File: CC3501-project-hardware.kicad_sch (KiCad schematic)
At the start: 29 parts, among them J1 USB_C_Receptacle_USB2.0_16P, J3 Conn_01x03_Socket, Q1 AO3400A, U1 RP2040, U4 SY8089A1AAC

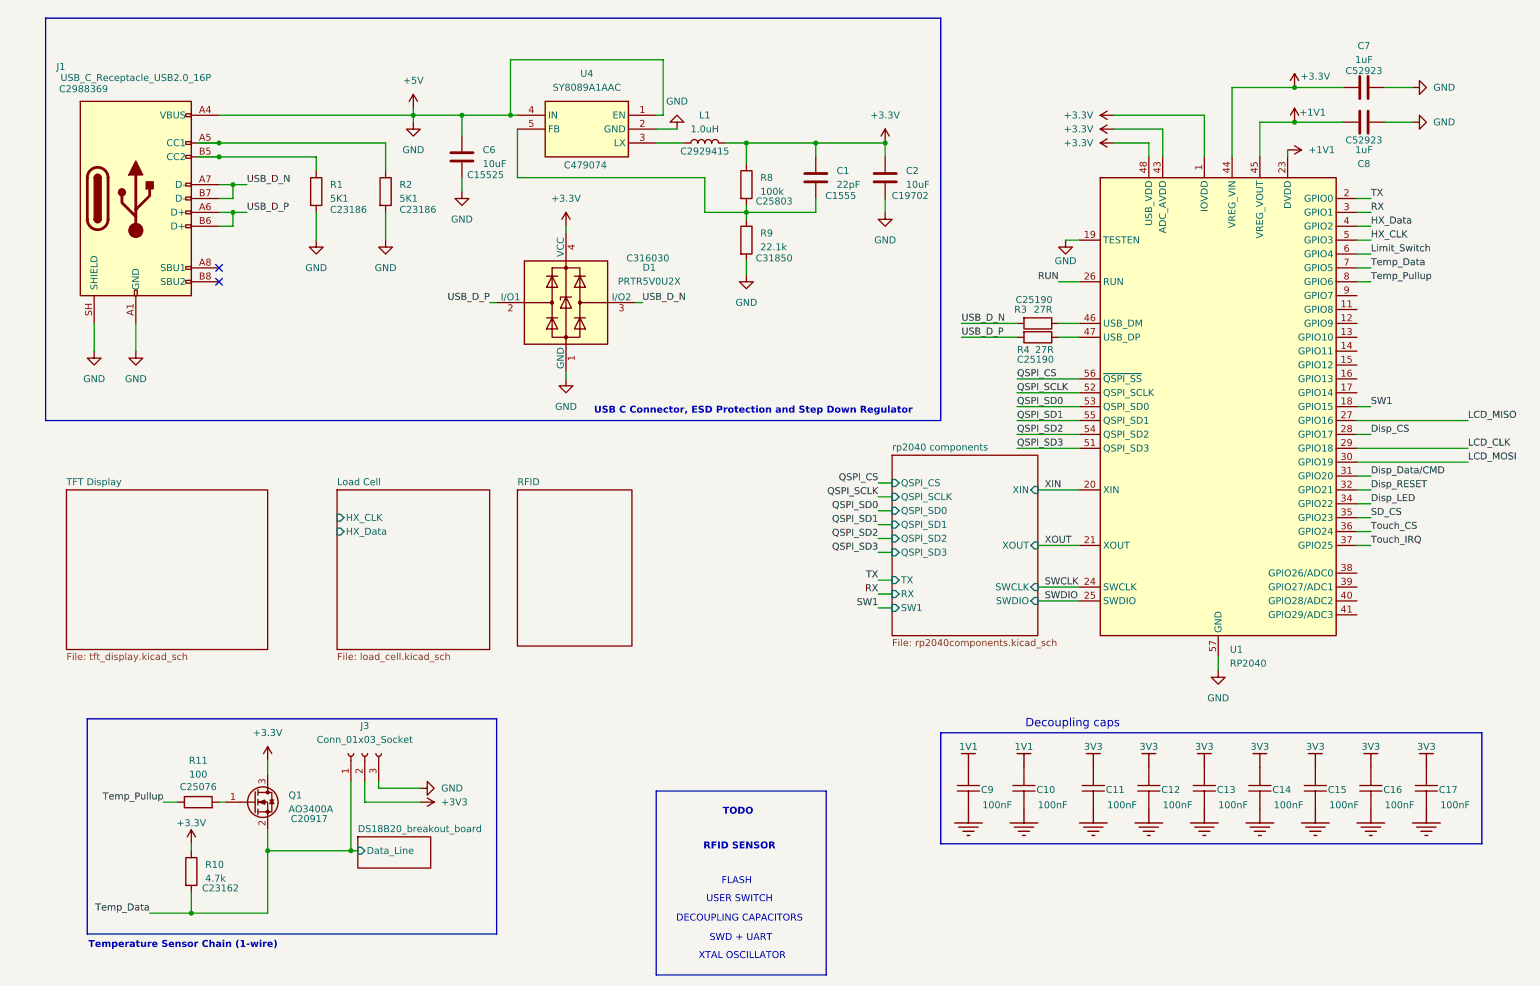
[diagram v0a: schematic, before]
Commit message: Attached part number to components.
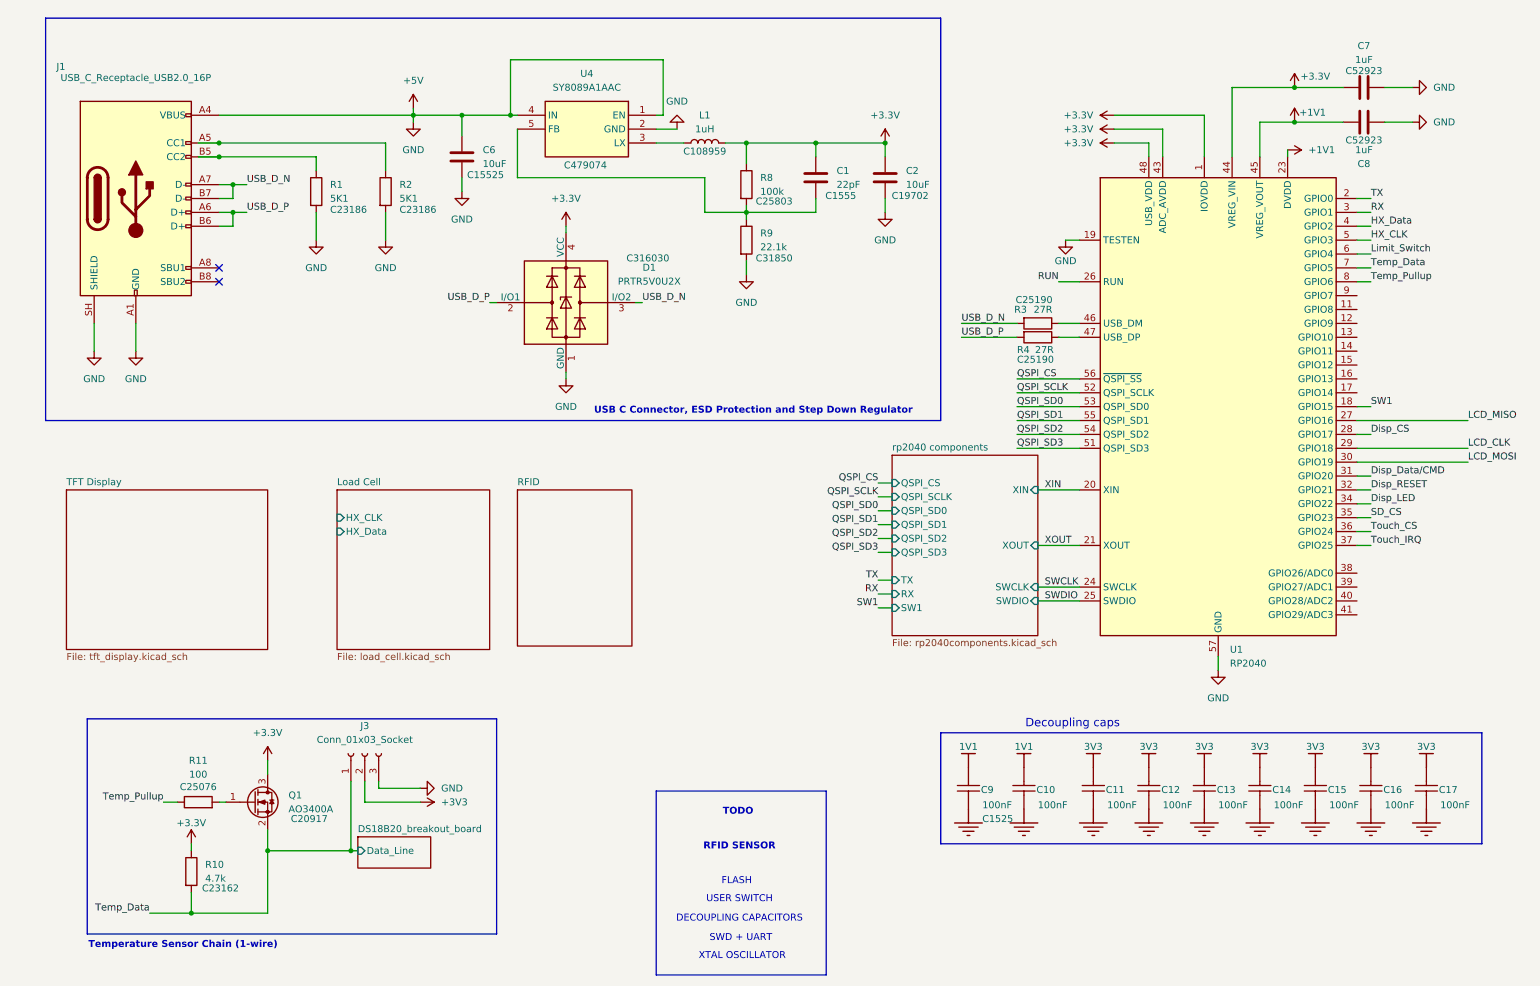
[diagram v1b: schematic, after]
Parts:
- C10, C11, C12, C13, C14, C15, C16, C17, C9: value CL05B104KO5NNNC -> 100nF
- J1: footprint Connector_USB:USB_C_Receptacle_G-Switch_GT-USB-7010ASV -> Connector_PinSocket_2.54mm:PinSocket_1x03_P2.54mm_Vertical; LCSC PN C2988369 -> (none)
- L1: value 1.0uH -> 1uH; footprint SamacSys_Parts:IND-SMD_L4.5-W4.0 -> Inductor_SMD:L_0603_1608Metric; LCSC PN C2929415 -> C108959
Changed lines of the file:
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@@
 			)
 		)
-		(property "Value" "CL05B104KO5NNNC"
+		(property "Value" "100nF"
 			(at 196.85 166.37 0)
 			(hide yes)
@@
 			)
 		)
-		(property "Value" "CL05B104KO5NNNC"
+		(property "Value" "100nF"
 			(at 270.51 166.37 0)
 			(hide yes)
@@
 	)
 	(symbol
+		(lib_name "root_1_CAP-NP-2_James Cook University_1")
 		(lib_id "James Cook University:root_1_CAP-NP-2_James Cook University")
 		(at 182.88 158.75 0)
@@
 			)
 		)
-		(property "Value" "CL05B104KO5NNNC"
+		(property "Value" "100nF"
 			(at 186.69 166.37 0)
 			(hide yes)
@@
 		)
 		(property "LCSC PN" "C1525"
-			(at 182.88 158.75 0)
-			(hide yes)
+			(at 185.42 160.528 0)
 			(show_name no)
 			(do_not_autoplace no)
@@
 					(size 1.27 1.27)
 				)
+				(justify left)
 			)
 		)
@@
 			)
 		)
-		(property "Value" "CL05B104KO5NNNC"
+		(property "Value" "100nF"
 			(at 240.03 166.37 0)
 			(hide yes)
@@
 			)
 		)
-		(property "Value" "CL05B104KO5NNNC"
+		(property "Value" "100nF"
 			(at 209.55 166.37 0)
 			(hide yes)
@@
 			)
 		)
-		(property "Value" "CL05B104KO5NNNC"
+		(property "Value" "100nF"
 			(at 229.87 166.37 0)
 			(hide yes)
@@
 			)
 		)
-		(property "Value" "CL05B104KO5NNNC"
+		(property "Value" "100nF"
 			(at 219.71 166.37 0)
 			(hide yes)
@@
 			)
 		)
-		(property "Value" "CL05B104KO5NNNC"
+		(property "Value" "100nF"
 			(at 250.19 166.37 0)
 			(hide yes)
@@
 			)
 		)
-		(property "Value" "CL05B104KO5NNNC"
+		(property "Value" "100nF"
 			(at 260.35 166.37 0)
 			(hide yes)
@@
 			)
 		)
-		(property "Value" "1.0uH"
+		(property "Value" "1uH"
 			(at 134.62 34.29 90)
 			(show_name no)
@@
 			)
 		)
-		(property "Footprint" "SamacSys_Parts:IND-SMD_L4.5-W4.0"
+		(property "Footprint" "Inductor_SMD:L_0603_1608Metric"
 			(at 134.62 36.83 0)
 			(hide yes)
@@
 			)
 		)
-		(property "LCSC PN" "C2929415"
+		(property "LCSC PN" "C108959"
 			(at 134.62 38.354 90)
 			(show_name no)
@@
 			)
 		)
-		(property "Footprint" "Connector_USB:USB_C_Receptacle_G-Switch_GT-USB-7010ASV"
+		(property "Footprint" "Connector_PinSocket_2.54mm:PinSocket_1x03_P2.54mm_Vertical"
 			(at 34.29 46.99 0)
 			(hide yes)
@@
 			)
 		)
-		(property "LCSC PN" "C2988369"
+		(property "LCSC PN" ""
 			(at 25.4 27.686 0)
 			(show_name no)

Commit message: Fix ERC errors.
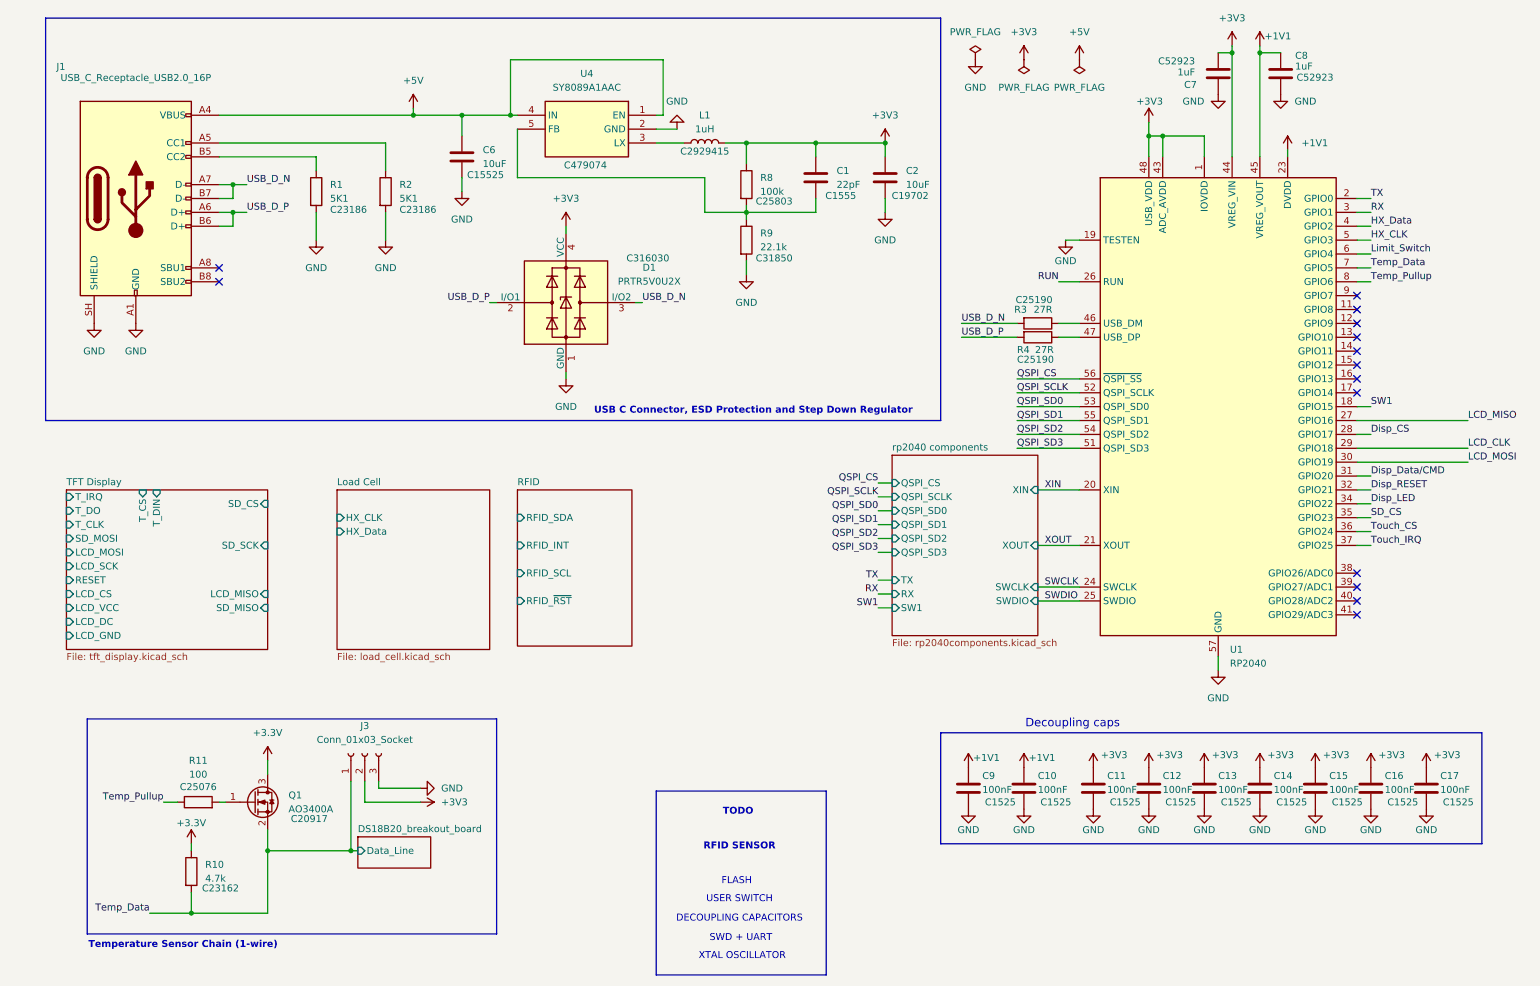
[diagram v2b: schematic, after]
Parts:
- removed C10, C11, C12, C13, C14, C15, C16, C17, C9: 100nF, Capacitor_SMD:C_0402_1005Metric, symbol James Cook University:root_1_CAP-NP-2_James Cook University
- added C10, C11, C12, C13, C14, C15, C16, C17, C9: 100nF, Capacitor_SMD:C_0402_1005Metric, symbol Device:C
- L1: footprint Inductor_SMD:L_0603_1608Metric -> SamacSys_Parts:IND-SMD_L4.5-W4.0; LCSC PN C108959 -> C2929415
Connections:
- net +1V1: now also C8.2, C10.1, C9.1; no longer C8.1
- net +3.3V: no longer C1.1, C2.1, C7.2, D1.4 (VCC), L1.1, R8.1, U1.1 (IOVDD), U1.10 (IOVDD), U1.22 (IOVDD), U1.33 (IOVDD), U1.42 (IOVDD), U1.43 (ADC_AVDD), U1.44 (VREG_VIN), U1.48 (USB_VDD), U1.49 (IOVDD)
- net +3V3: now also C1.1, C2.1, C7.2, D1.4 (VCC), L1.1, R8.1, U1.1 (IOVDD), U1.10 (IOVDD), U1.22 (IOVDD), U1.33 (IOVDD), U1.42 (IOVDD), U1.43 (ADC_AVDD), U1.44 (VREG_VIN), U1.48 (USB_VDD), U1.49 (IOVDD), C11.1, C12.1, C13.1, C14.1, C15.1, C16.1, C17.1
- net +5V: no longer C2.2, C6.2, C7.1, C8.2, D1.1 (GND), J1.A1 (GND), J1.A12 (GND), J1.B1 (GND), J1.B12 (GND), J1.SH (SHIELD), J3.3 (Pin_3), R1.2, R2.2, R9.2, U1.19 (TESTEN), U1.57 (GND), U4.2 (GND)
- new net GND: C10.2, C11.2, C12.2, C13.2, C14.2, C15.2, C16.2, C17.2, C2.2, C6.2, C7.1, C8.1, C9.2, D1.1 (GND), J1.A1 (GND), J1.A12 (GND), J1.B1 (GND), J1.B12 (GND), J1.SH (SHIELD), J3.3 (Pin_3), R1.2, R2.2, R9.2, U1.19 (TESTEN), U1.57 (GND), U4.2 (GND)
- no-connect marks 2 -> 14
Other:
- sheet RFID ports: added RFID_INT, RFID_SCL, RFID_SDA, RFID_~{RST}; removed none
- sheet TFT Display ports: added LCD_CS, LCD_DC, LCD_GND, LCD_MISO, LCD_MOSI, LCD_SCK, LCD_VCC, RESET, SD_CS, SD_MISO, SD_MOSI, SD_SCK, T_CLK, T_CS, T_DIN, T_DO, T_IRQ; removed none
- moved on the sheet: C7, C8

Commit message: Fix ERC errors.
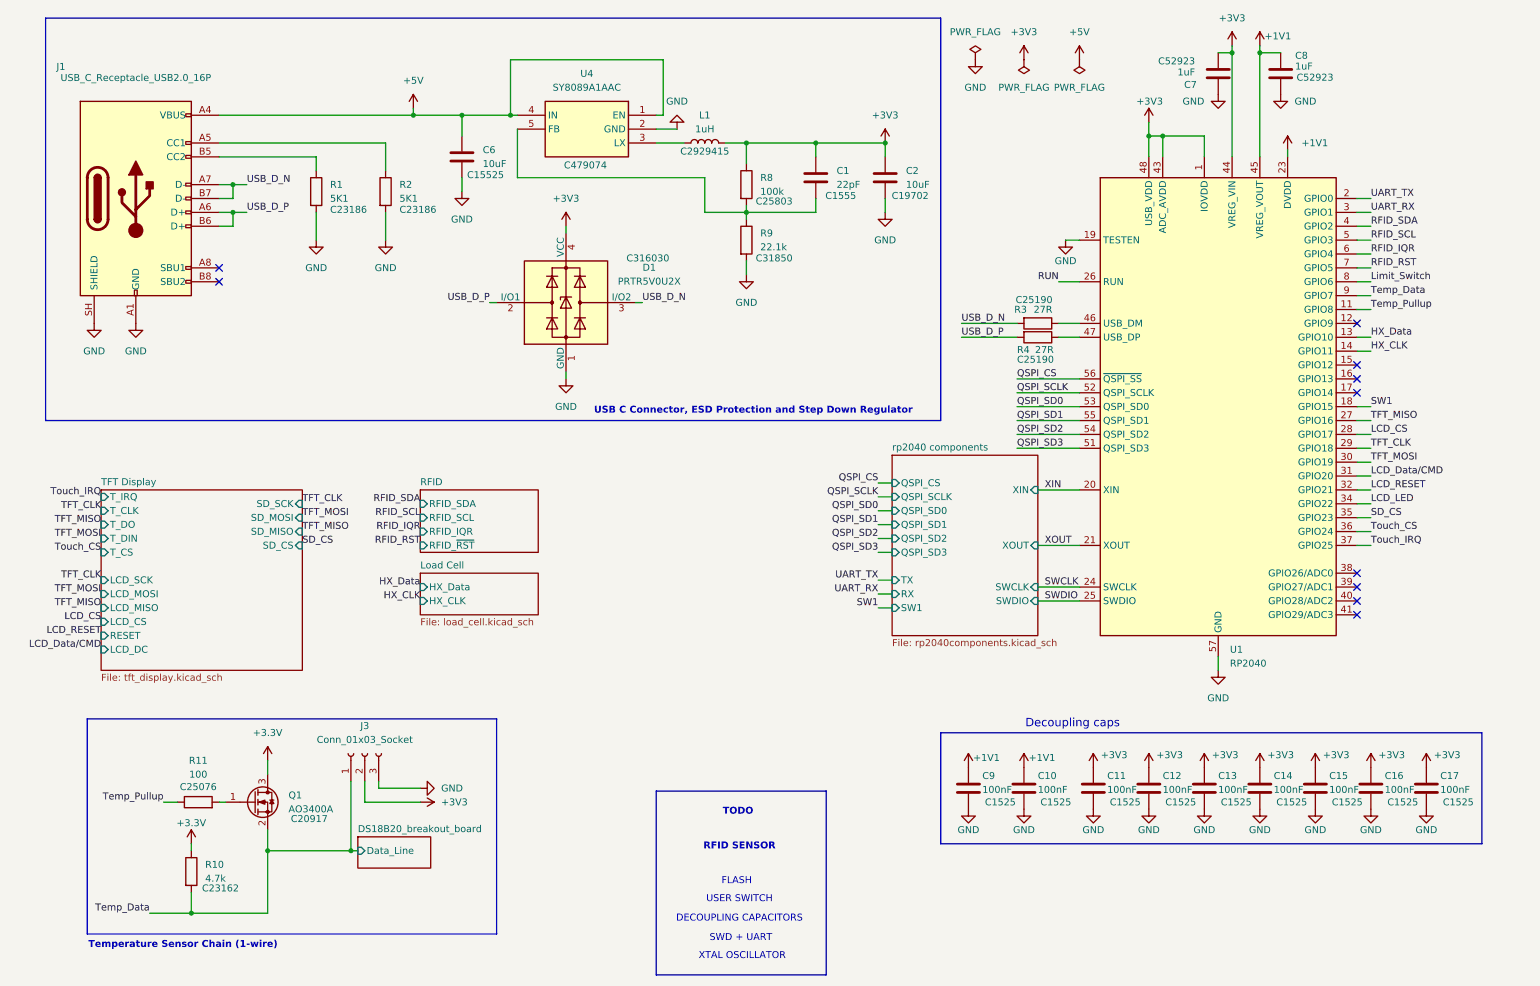
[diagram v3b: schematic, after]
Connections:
- net HX_CLK: now also U1.14 (GPIO11); no longer U1.5 (GPIO3)
- net HX_Data: now also U1.13 (GPIO10); no longer U1.4 (GPIO2)
- net Limit_Switch: now also U1.8 (GPIO6); no longer U1.6 (GPIO4)
- net Temp_Data: now also U1.9 (GPIO7); no longer U1.7 (GPIO5)
- net Temp_Pullup: now also U1.11 (GPIO8); no longer U1.8 (GPIO6)
- net Disp_CS renamed LCD_CS
- net Disp_Data/CMD renamed LCD_Data/CMD
- net Disp_LED renamed LCD_LED
- net Disp_RESET renamed LCD_RESET
- net LCD_CLK renamed TFT_CLK
- net LCD_MISO renamed TFT_MISO
- net LCD_MOSI renamed TFT_MOSI
- net RX renamed UART_RX
- net TX renamed UART_TX
- new net RFID_IQR: U1.6 (GPIO4)
- new net RFID_RST: U1.7 (GPIO5)
- new net RFID_SCL: U1.5 (GPIO3)
- new net RFID_SDA: U1.4 (GPIO2)
- no-connect marks 14 -> 10
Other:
- sheet RFID: file RFID/CE-PiicoDev-RFID-Reader-Writer.kicad_sch -> RFID\CE-PiicoDev-RFID-Reader-Writer.kicad_sch
- sheet RFID ports: added RFID_IQR; removed RFID_INT
- sheet TFT Display ports: added none; removed LCD_GND, LCD_VCC
